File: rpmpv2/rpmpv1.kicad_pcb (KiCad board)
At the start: 2 copper layers, 65.1 x 64.4 mm, 12 parts, among them J1 RPi_GPIO, J2 RPi_GPIO, P1 CONN_02X25, U1 74LS05, U2 74LS245, U3 74LS245, U4 74LS08, U5 74LS245, U6 74HC244

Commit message: RPMP V2 updated
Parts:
- added R2: R, Resistors_SMD:R_0603_HandSoldering, F.Cu at (177.8, 97.3)
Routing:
- net +5V: track 148.7 -> 26.2 mm, vias 2 -> 0
- net GND: track 78.0 -> 0.00 mm, vias 14 -> 0
- net /nWR0: track 62.5 -> 0.00 mm, vias 2 -> 0
- net /RA13: track 74.2 -> 22.9 mm, vias 1 -> 0
- net /IORQ: track 48.9 -> 0.00 mm, vias 1 -> 0
- net /RA12: track 71.4 -> 23.5 mm, vias 1 -> 0
- net /A6: track 43.0 -> 0.00 mm
- net /SLTSL: track 42.3 -> 0.00 mm, vias 3 -> 0
- net /LE_D: track 42.2 -> 0.00 mm
- net /RS2: track 116.1 -> 76.3 mm
- net /RESET: track 37.8 -> 0.00 mm, vias 1 -> 0
- net /A7: track 36.8 -> 0.00 mm, vias 1 -> 0
- net /RA8: track 59.3 -> 22.9 mm
- net /nIORQ: track 35.5 -> 0.00 mm, vias 1 -> 0
- net /RD: track 34.4 -> 0.00 mm, vias 2 -> 0
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
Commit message: logic update for better control
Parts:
- removed R2, R3: R, Resistors_SMD:R_0603_HandSoldering
- removed U6: 74HC244, Housings_SOIC:SOIC-20W_7.5x12.8mm_Pitch1.27mm
- U1: moved to B.Cu
- U4: value 74LS08 -> 74LS245; footprint Housings_SOIC:SOIC-14_3.9x8.7mm_Pitch1.27mm -> Housings_SOIC:SOIC-20W_7.5x12.8mm_Pitch1.27mm; moved to F.Cu
- moved R1 28.2 mm to (157.5, 87.6), turned to 180 degrees
- moved U1 20.5 mm to (157.5, 94.0), turned to 0 degrees
- moved J1 13.7 mm to (195.3, 76.3)
- moved U2 9.98 mm to (172.7, 94.0)
- moved U4 5.68 mm to (172.7, 94.0), turned to 270 degrees
- moved U3 2.65 mm to (142.2, 94.0)
- moved U5 2.65 mm to (142.2, 94.0)
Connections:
- net /RS2 renamed /RC26
- net /RS3 renamed /RC27
- J1 pad 10: /RA7 -> /RA15
- J1 pad 11: /RA9 -> /RC17
- J1 pad 12: /RA10 -> /RC18
- J1 pad 15: /RA14 -> /RC22
- J1 pad 16: /RA15 -> /RC23
- J1 pad 18: /RS0 -> /RC24
- J1 pad 19: /RA2 -> /RA10
- J1 pad 21: /RA1 -> /RA9
- J1 pad 22: /RS1 -> /RC25
- J1 pad 23: /RA3 -> /RA11
- J1 pad 24: /RA0 -> /RA8
- J1 pad 32: /RA4 -> /RA12
- J1 pad 33: /RA5 -> /RA13
- J1 pad 35: /RA11 -> /RC19
- J1 pad 36: /RA8 -> /RC16
- J1 pad 38: /RA12 -> /RC20
- J1 pad 40: /RA13 -> /RC21
- J1 pad 8: /RA6 -> /RA14
- J2 pad 10: /RA7 -> /RA15
- J2 pad 11: /RA9 -> /RC17
- J2 pad 12: /RA10 -> /RC18
- J2 pad 15: /RA14 -> /RC22
- J2 pad 16: /RA15 -> /RC23
- J2 pad 18: /RS0 -> /RC24
- J2 pad 19: /RA2 -> /RA10
- J2 pad 21: /RA1 -> /RA9
- J2 pad 22: /RS1 -> /RC25
- J2 pad 23: /RA3 -> /RA11
- J2 pad 24: /RA0 -> /RA8
- J2 pad 32: /RA4 -> /RA12
- J2 pad 33: /RA5 -> /RA13
- J2 pad 35: /RA11 -> /RC19
- J2 pad 36: /RA8 -> /RC16
- J2 pad 38: /RA12 -> /RC20
- J2 pad 40: /RA13 -> /RC21
- J2 pad 8: /RA6 -> /RA14
- R1 pad 1: +5V -> /nRC24
- R1 pad 2: /nWR0 -> +5V
- U1 pad 10: /nIORQ -> /nRC24
- U1 pad 11: /IORQ -> /RC24
- U1 pad 12: /nWR0 -> (no net)
- U1 pad 13: /WR0 -> (no net)
- U2 pad 19: /nIORQ -> GND
- U3 pad 1: /nWR0 -> /RC25
- U3 pad 19: /LE_D -> /nRC24
- U4 pad 1: /SLTSL -> GND
- U4 pad 10: (no net) -> GND
- U4 pad 11: (no net) -> /SLTSL
- U4 pad 12: (no net) -> /IORQ
- U4 pad 13: (no net) -> /RD
- U4 pad 14: +5V -> /RESET
- U4 pad 2: /IORQ -> /BDIR0
- U4 pad 3: /LE_D -> /RST0
- U4 pad 4: /RD -> /INT0
- U4 pad 5: /BUSDIR -> /WAIT0
- U4 pad 6: /WR0 -> /RC19
- U4 pad 7: GND -> /RC18
- U4 pad 8: (no net) -> /RC17
- U4 pad 9: (no net) -> /RC16
- U5 pad 1: GND -> /RC24
- U5 pad 2: /RA1 -> /RD1
- U5 pad 3: /RA0 -> /RD0
- U5 pad 4: /RA3 -> /RD3
- U5 pad 5: /RA2 -> /RD2
- U5 pad 6: /RA5 -> /RD5
- U5 pad 7: /RA4 -> /RD4
- U5 pad 8: /RA7 -> /RD7
- U5 pad 9: /RA6 -> /RD6
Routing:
- net /RC26: track 76.3 -> 0.00 mm
- net /RA6: track 71.1 -> 0.00 mm
- net +3V3: track 69.9 -> 0.00 mm
- net /RD2: track 65.2 -> 0.00 mm
- net /RA7: track 58.4 -> 0.00 mm, vias 1 -> 0
- net /RD3: track 54.7 -> 0.00 mm
- net /RA11: track 47.5 -> 0.00 mm, vias 1 -> 0
- net /RD4: track 39.1 -> 0.00 mm
- net /RA2: track 34.5 -> 0.00 mm
- net /RA5: track 28.9 -> 0.00 mm
- net /RA14: track 28.5 -> 0.00 mm
- net /RA9: track 26.8 -> 0.00 mm
- net /RA3: track 26.8 -> 0.00 mm
- net /RD0: track 26.8 -> 0.00 mm
- net /RA1: track 26.8 -> 0.00 mm
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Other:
- board size 65.1 x 64.4 mm -> 85.7 x 64.4 mm

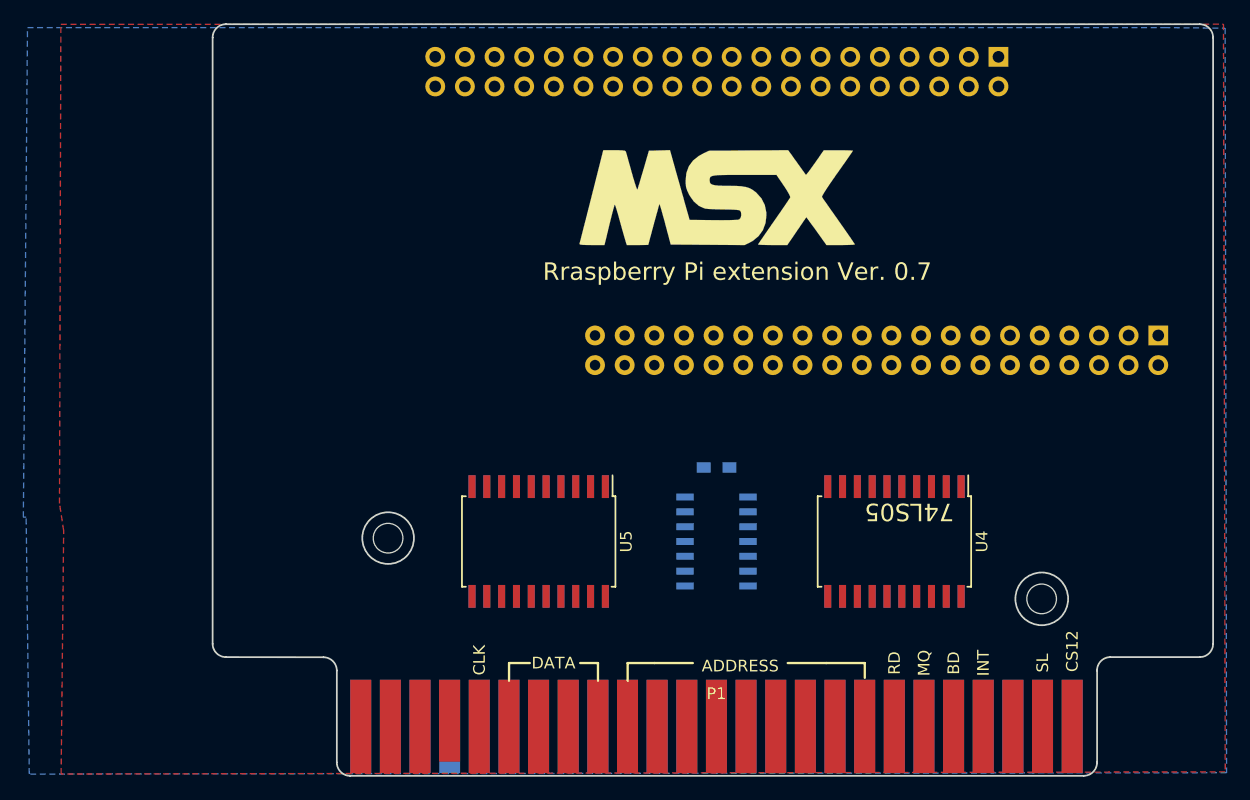
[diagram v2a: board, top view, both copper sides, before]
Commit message: address injuection feature
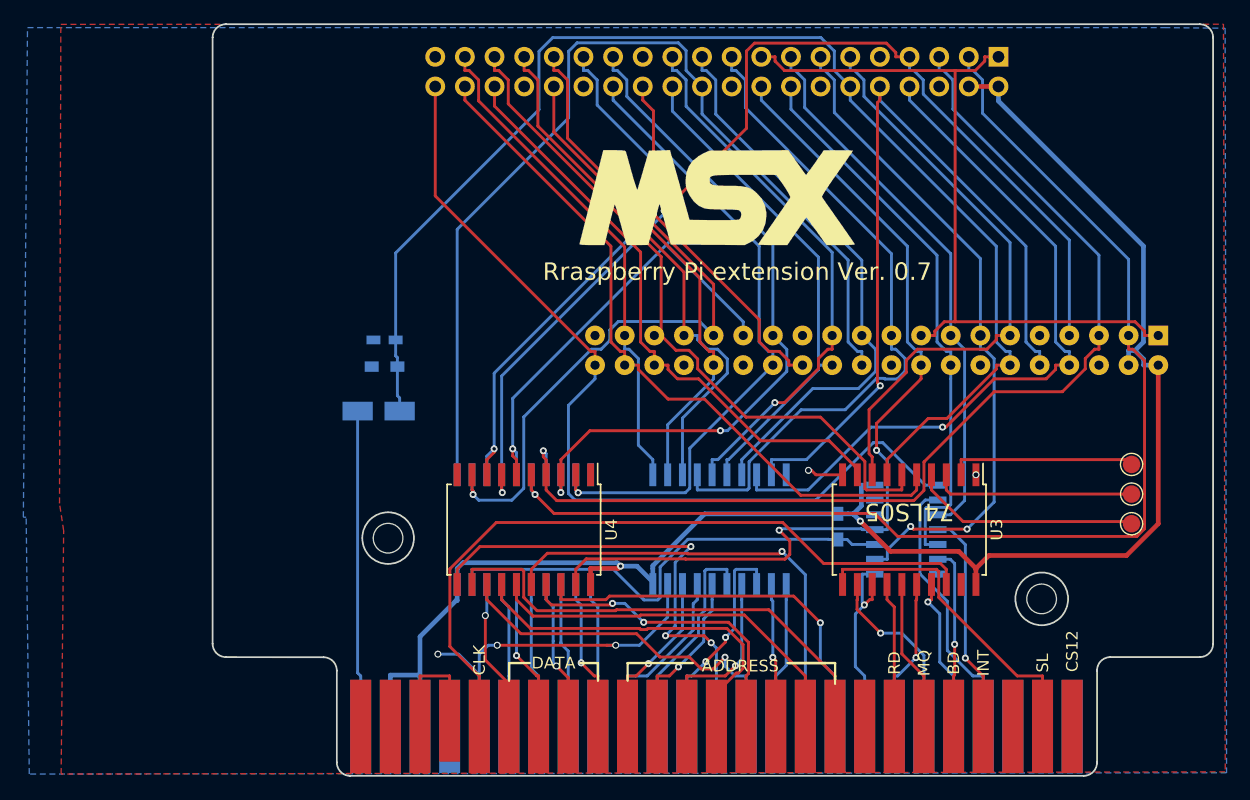
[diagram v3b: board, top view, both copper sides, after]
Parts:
- added C1: C, Capacitors_SMD:C_0603_HandSoldering, B.Cu at (129.0, 76.7)
- added C2: CP, Capacitors_SMD:CP_Elec_4x5.3, B.Cu at (128.5, 82.8)
- added J3: TEST_1P, TestPoint:TestPoint_Pad_D1.5mm, F.Cu at (193.0, 92.5)
- added J4: TEST_1P, TestPoint:TestPoint_Pad_D1.5mm, F.Cu at (193.0, 89.9)
- added J5: TEST_1P, TestPoint:TestPoint_Pad_D1.5mm, F.Cu at (193.0, 87.4)
- added R2: R, Resistors_SMD:R_0603_HandSoldering, B.Cu at (129.0, 79.0)
- U1: value 74LS05 -> 74LS245; footprint Housings_SOIC:SOIC-14_3.9x8.7mm_Pitch1.27mm -> Housings_SOIC:SOIC-20W_7.5x12.8mm_Pitch1.27mm
- U3: moved to F.Cu
- U5: value 74LS245 -> 74LS05; footprint Housings_SOIC:SOIC-20W_7.5x12.8mm_Pitch1.27mm -> Housings_SOIC:SOIC-14_3.9x8.7mm_Pitch1.27mm; moved to B.Cu
- moved U2 31.8 mm to (141.0, 93.0)
- moved U3 31.8 mm to (174.0, 93.0)
- moved U4 31.8 mm to (141.0, 93.0)
- moved U5 31.5 mm to (173.7, 93.0), turned to 180 degrees
- moved R1 11.6 mm to (167.9, 92.7), turned to 90 degrees
- moved U1 1.05 mm to (157.7, 93.0), turned to 270 degrees
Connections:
- U1 pad 1: /WAIT0 -> /RC26
- U1 pad 10: /nRC24 -> GND
- U1 pad 11: /RC24 -> /A7
- U1 pad 12: (no net) -> /A6
- U1 pad 13: (no net) -> /A1
- U1 pad 14: +5V -> /A0
- U1 pad 2: /WAIT -> /RA12
- U1 pad 3: /INT0 -> /RA13
- U1 pad 4: /INT -> /RA10
- U1 pad 5: /BDIR0 -> /RA11
- U1 pad 6: /BUSDIR -> /RA8
- U1 pad 7: GND -> /RA9
- U1 pad 8: /RESET -> /RA14
- U1 pad 9: /RST0 -> /RA15
- U2 pad 1: GND -> /RC25
- U2 pad 11: /A15 -> /D1
- U2 pad 12: /A9 -> /D0
- U2 pad 13: /A11 -> /D3
- U2 pad 14: /A10 -> /D2
- U2 pad 15: /A12 -> /D5
- U2 pad 16: /A8 -> /D4
- U2 pad 17: /A14 -> /D7
- U2 pad 18: /A13 -> /D6
- U2 pad 19: GND -> /nRC24
- U2 pad 2: /RA13 -> /RD6
- U2 pad 3: /RA14 -> /RD7
- U2 pad 4: /RA8 -> /RD4
- U2 pad 5: /RA12 -> /RD5
- U2 pad 6: /RA10 -> /RD2
- U2 pad 7: /RA11 -> /RD3
- U2 pad 8: /RA9 -> /RD0
- U2 pad 9: /RA15 -> /RD1
- U3 pad 1: /RC25 -> GND
- U3 pad 11: /D1 -> /SLTSL
- U3 pad 12: /D0 -> /IORQ
- U3 pad 13: /D3 -> /RESET
- U3 pad 14: /D2 -> /RD
- U3 pad 15: /D5 -> /MREQ
- U3 pad 16: /D4 -> /WR
- U3 pad 17: /D7 -> /M1
- U3 pad 18: /D6 -> /CLK
- U3 pad 19: /nRC24 -> GND
- U3 pad 2: /RD6 -> /TP2
- U3 pad 3: /RD7 -> /TP1
- U3 pad 4: /RD4 -> /TP0
- U3 pad 5: /RD5 -> /RC20
- U3 pad 6: /RD2 -> /RC19
- U3 pad 7: /RD3 -> /RC18
- U3 pad 8: /RD0 -> /RC17
- U3 pad 9: /RD1 -> /RC16
- U4 pad 11: /SLTSL -> /A14
- U4 pad 12: /IORQ -> /A15
- U4 pad 13: /RD -> /A12
- U4 pad 14: /RESET -> /A13
- U4 pad 15: /RC20 -> /A10
- U4 pad 16: /RC21 -> /A11
- U4 pad 17: /RC22 -> /A8
- U4 pad 18: /RC23 -> /A9
- U4 pad 19: GND -> /RC24
- U4 pad 2: /BDIR0 -> /RD1
- U4 pad 3: /RST0 -> /RD0
- U4 pad 4: /INT0 -> /RD3
- U4 pad 5: /WAIT0 -> /RD2
- U4 pad 6: /RC19 -> /RD5
- U4 pad 7: /RC18 -> /RD4
- U4 pad 8: /RC17 -> /RD7
- U4 pad 9: /RC16 -> /RD6
- U5 pad 1: /RC24 -> /RC21
- U5 pad 10: GND -> /nRC24
- U5 pad 11: /A6 -> /RC24
- U5 pad 12: /A7 -> (no net)
- U5 pad 13: /A4 -> (no net)
- U5 pad 14: /A5 -> +5V
- U5 pad 2: /RD1 -> /WAIT
- U5 pad 3: /RD0 -> /RC22
- U5 pad 4: /RD3 -> /INT
- U5 pad 5: /RD2 -> /RC23
- U5 pad 6: /RD5 -> /BUSDIR
- U5 pad 7: /RD4 -> GND
- U5 pad 8: /RD7 -> /RESET
- U5 pad 9: /RD6 -> /RC27
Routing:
- net +5V: track 0.00 -> 147.9 mm, vias 0 -> 2
- net /RC18: track 0.00 -> 111.1 mm
- net /RD2: track 0.00 -> 104.7 mm, vias 0 -> 1
- net /RD4: track 0.00 -> 92.8 mm, vias 0 -> 2
- net /RD3: track 0.00 -> 91.6 mm, vias 0 -> 1
- net /RC25: track 0.00 -> 84.3 mm
- net /RC24: track 0.00 -> 77.8 mm, vias 0 -> 2
- net /RC21: track 0.00 -> 77.1 mm
- net /RA15: track 0.00 -> 68.8 mm, vias 0 -> 1
- net +3V3: track 0.00 -> 65.0 mm
- net /RD6: track 0.00 -> 65.0 mm, vias 0 -> 1
- net /RA14: track 0.00 -> 62.5 mm, vias 0 -> 1
- net /CLK: track 0.00 -> 61.7 mm
- net /RD7: track 0.00 -> 61.5 mm, vias 0 -> 2
- net /RC20: track 0.00 -> 61.1 mm
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
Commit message: update for PCB order
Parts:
- moved G*** 3.43 mm to (154.1, 64.4)
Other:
- board text added: "2018.03.01"
- board text added: "74HC05"
- board text added: "74HC245"
- board text added: "BDIR"
- board text removed: "2018.01.19"
- board text removed: "74LS05"
- board text removed: "BD"
